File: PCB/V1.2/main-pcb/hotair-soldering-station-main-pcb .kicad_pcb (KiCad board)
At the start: 2 copper layers, 90 x 91 mm, 102 parts, among them J1 230VAC_IN, J10 T12_power (NS-25 r2,54), J11 LCD_CON2 (JST r.2.0), J12 LCD_CON1 (JST r.2.0), J13 ICP (goldpin r2,54), J14 T12_signal (NS-25 r2,54), J2 FRONT_PANEL (IDC r. 2,54), J3 EARTH_GND, J4 24V_IN (NS-25 r2,54), J5 PSUPPLY (PWZ-02S r.3,96), J6 HOTAIR_FAN (JST r,2,54), J7 HOTAIR_MEAS (JST r.2,5), J8 HOTAIR_HEATER (PWZ-02S r.3,96), J9 WEP (r.2,54), Q1 BC817, Q10 FP3055LP, Q11 BC817, Q2 BC807, Q3 BC817, Q4 Q_PMOS_GDS, Q5 BC817, Q6 BT139-600, Q7 BC817, Q8 FP3055LP, Q9 BC817, U1 MOC3041M, U2 MAX31855KASA, U3 MP1584-Step-Down, U4 AP1117-ADJ, U6 LM358, U7 MAX31855KASA, U8 STM32F103C6Tx

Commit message: Schematic and PCB update
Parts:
- removed F2: Polyfuse, Fuse:Fuse_Bourns_MF-RG500
- removed J14: T12_signal (NS-25 r2,54), Connector:Conn-01x03-N25-W4P
- removed U7: MAX31855KASA, Package_SO:SOIC-8_3.9x4.9mm_P1.27mm
- added C17: 10n, Capacitors:0805, F.Cu at (76.9, 99.7)
- added C21: 10n, Capacitors:0805, F.Cu at (84.9, 99.9)
- added C22: 100n, Capacitors:0603, F.Cu at (77.0, 94.6)
- added D1: 1N4148, Diode_SMD:D_MiniMELF, F.Cu at (161.2, 64.5)
- added D10: 1N4148, Diode_SMD:D_MiniMELF, F.Cu at (161.2, 61.3)
- added D11: 3V6, Diode_SMD:D_MiniMELF, F.Cu at (172.6, 42.0)
- added D12: SR310, Diode_SMD:D_SMA, F.Cu at (161.5, 44.7)
- added D2: 1N4148, Diode_SMD:D_MiniMELF, F.Cu at (154.8, 64.5)
- added D3: 3V6, Diode_SMD:D_MiniMELF, F.Cu at (161.1, 53.0)
- added D4: 12V, Diode_SMD:D_0805_2012Metric, F.Cu at (166.0, 51.5)
- added D6: SR310, Diode_SMD:D_SMA, F.Cu at (125.6, 42.1)
- added D8: 1N4148, Diode_SMD:D_MiniMELF, F.Cu at (154.8, 61.3)
- added D9: 12V, Diode_SMD:D_0805_2012Metric, F.Cu at (167.7, 48.4)
- added Q12: BC817, Package_TO_SOT_SMD:SOT-23, F.Cu at (161.3, 49.2)
- added Q13: BC817, Package_TO_SOT_SMD:SOT-23, F.Cu at (168.3, 38.2)
- added Q14: BC807, Package_TO_SOT_SMD:SOT-23, F.Cu at (167.9, 44.7)
- added Q15: RFP15P05, My-Footprints:TO-220-3_V_Thick_Pads, B.Cu at (112.3, 68.6)
- added R41: 1k5, Capacitors:0805, F.Cu at (64.6, 111.8)
- added R42: 430R, Capacitors:0805, F.Cu at (65.5, 106.0)
- added R43: 2k2, Capacitors:0805, F.Cu at (84.9, 97.3)
- added R44: 10k, Capacitors:0805, F.Cu at (72.7, 108.6)
- added R45: 10k, Capacitors:0805, F.Cu at (80.9, 97.3)
- added R46: 1k5, Capacitors:0805, F.Cu at (60.5, 109.1)
- added R47: 430R, Capacitors:0805, F.Cu at (85.1, 94.7)
- added R48: 1k, Capacitors:0805, F.Cu at (89.2, 94.7)
- added R49: 200k, Capacitors:0805, F.Cu at (76.9, 102.4)
- added R50: 100R, Capacitors:0805, F.Cu at (64.6, 109.1)
- added R51: 100k, Capacitors:0805, F.Cu at (73.6, 106.0)
- added R52: 10k, Capacitors:0805, F.Cu at (81.7, 105.2)
- added R53: 10k, Capacitors:0805, F.Cu at (84.9, 102.6)
- added R54: 10k, Capacitors:0805, F.Cu at (68.6, 108.6)
- added R55: 10k, Capacitors:0805, F.Cu at (76.9, 97.1)
- added R56: 47k, Capacitors:0805, F.Cu at (60.5, 111.8)
- C15: value 330u/35V -> 10n; footprint Capacitors_ThroughHole:CP_Radial_D10.0mm_P5.00mm -> Capacitors:0805; moved to F.Cu
- F1: value 3,15A -> 1,5A
- J3: footprint My-Footprints:Screw-Terminal-5.00mm-2pin -> My-Footprints:Screw-Terminal-5.00mm-3pin; moved to F.Cu
- Q10: value FP3055LP -> RFP15P05; footprint Package_TO_SOT_THT:TO-220-3_Vertical -> My-Footprints:TO-220-3_V_Thick_Pads
- Q4: value Q_PMOS_GDS -> RFP15P05
- Q8: value FP3055LP -> BC807; footprint Package_TO_SOT_THT:TO-220-3_Vertical -> Package_TO_SOT_SMD:SOT-23; moved to F.Cu
- R1: value 0R -> 47k
- R14: value xx -> 33k
- R15: value xx -> 2k2
- R16: value 0R -> 1M
- R18, R30: value 1k -> 10k
- R19: value 10k -> 1k
- R20: value 4,7k -> 2k2
- R24: value 1k -> 100k
- R27: moved to F.Cu
- R28: value 4,7k -> 200k
- R29: value 10k -> 2k2
- R32: value 100R -> 10k
- R35: value 10k -> 1M
- R36: value 1k -> 2k2
- R38: value xx -> 24k
- R40: value xx -> 2k
- moved D5 80.5 mm to (137.0, 101.6)
- moved U2 76.6 mm to (161.7, 39.2), turned to 0 degrees
- moved Q5 75.7 mm to (173.2, 38.2)
- moved R27 75.3 mm to (60.1, 106.2)
- moved J3 67.7 mm to (59.3, 94.1)
- moved LS1 64.2 mm to (62.8, 53.5), turned to -90 degrees
- moved C15 63.3 mm to (80.9, 99.9), turned to 0 degrees
- moved G*** 61.7 mm to (156.7, 81.9)
- moved R30 60.8 mm to (69.5, 106.0), turned to 0 degrees
- moved R28 60.3 mm to (68.6, 111.3), turned to 0 degrees
- moved U6 55.0 mm to (121.7, 89.9), turned to 90 degrees
- moved R32 54.3 mm to (77.6, 105.2), turned to 0 degrees
- moved C6 53.5 mm to (141.9, 92.2)
- moved C12 53.5 mm to (129.5, 99.3)
- moved C13 53.5 mm to (128.0, 99.3)
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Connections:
- C15 pad 1: +24V -> IRON_WEP_HEATER_CTRL
- C15 pad 2: GND2 -> Net-(Q7-Pad1)
- C3 pad 1: Net-(C3-Pad1) -> Net-(U6-Pad3)
- C4 pad 1: IRON_T12_THERM -> Net-(C4-Pad1)
- J10 pad 1: +24V -> Net-(J10-Pad1)
- J10 pad 2: +24V -> GND2
- J10 pad 3: IRON_T12_HEATER -> GND2
- J10 pad 4: IRON_T12_HEATER -> IRON_T12_THERM_HEATER
- J10 pad 5: IRON_T12_HEATER -> IRON_T12_THERM_HEATER
- J4 pad 3: Net-(F2-Pad2) -> +24V
- J4 pad 4: Net-(F2-Pad2) -> +24V
- J7 pad 3: HOTAIR_REED_SW -> Net-(J7-Pad3)
- J9 pad 1: +24V -> GND2
- J9 pad 2: +24V -> GND2
- J9 pad 5: IRON_WEP_THERM -> IRON_WEP_THERM+
- J9 pad 6: THERM_GND -> IRON_WEP_THERM-
- Q10 pad 1: Net-(Q10-Pad1) -> IRON_WEP_HEATER
- Q10 pad 2: IRON_T12_HEATER -> Net-(R24-Pad2)
- Q10 pad 3: GND2 -> +24V
- Q5 pad 1: Net-(Q5-Pad1) -> Net-(Q7-Pad3)
- Q5 pad 2: GND -> Net-(R25-Pad1)
- Q5 pad 3: Net-(Q5-Pad3) -> +24V
- Q7 pad 2: GND -> Net-(Q7-Pad2)
- Q8 pad 1: Net-(Q8-Pad1) -> Net-(Q7-Pad3)
- Q8 pad 2: IRON_WEP_HEATER -> Net-(R25-Pad1)
- Q8 pad 3: GND2 -> GND
- R1 pad 1: HOTAIR_THERM -> GND
- R1 pad 2: Net-(R1-Pad2) -> Net-(Q1-Pad1)
- R16 pad 1: HOTAIR_THERM -> +5V
- R16 pad 2: Net-(C3-Pad1) -> HOTAIR_THERM
- R18 pad 1: Net-(R18-Pad1) -> HOTAIR_THERM
- R18 pad 2: HOTAIR_TEMP_ADC -> Net-(U6-Pad3)
- R19 pad 1: +3V3 -> GND
- R19 pad 2: Net-(C3-Pad1) -> Net-(U6-Pad2)
- R24 pad 1: +5V -> +24V
- R24 pad 2: Net-(Q7-Pad3) -> Net-(R24-Pad2)
- R25 pad 1: Net-(Q8-Pad1) -> Net-(R25-Pad1)
- R25 pad 2: Net-(Q7-Pad3) -> Net-(R24-Pad2)
- R28 pad 1: Net-(Q5-Pad1) -> Net-(U6-Pad2)
- R28 pad 2: IRON_T12_HEATER_CTRL -> Net-(U6-Pad1)
- R29 pad 1: GND -> Net-(U6-Pad1)
- R29 pad 2: Net-(Q5-Pad1) -> HOTAIR_TEMP_ADC
- R30 pad 1: +5V -> HOTAIR_REED_SW
- R30 pad 2: Net-(Q5-Pad3) -> Net-(J7-Pad3)
- R32 pad 1: Net-(Q10-Pad1) -> Net-(J7-Pad3)
- R32 pad 2: Net-(Q5-Pad3) -> +5V
- R35 pad 1: +3V3 -> +5V
- R35 pad 2: IRON_T12_THERM -> IRON_T12_THERM_HEATER
- U2 pad 2: THERM_GND -> IRON_WEP_THERM-
- U2 pad 3: Net-(R1-Pad2) -> IRON_WEP_THERM+
- U2 pad 6: MAX31855_HOTAIR_CS -> MAX31855_IRON_CS
- U6 pad 1: Net-(R18-Pad1) -> Net-(U6-Pad1)
- U6 pad 2: Net-(R18-Pad1) -> Net-(U6-Pad2)
- U6 pad 3: Net-(C3-Pad1) -> Net-(U6-Pad3)
- U6 pad 5: IRON_T12_THERM -> Net-(C4-Pad1)
- U6 pad 6: Net-(R36-Pad1) -> Net-(U6-Pad6)
- U8 pad 14: MAX31855_HOTAIR_CS -> unconnected-(U8-Pad14)
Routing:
- net +3V3: track 187.0 -> 0.00 mm, vias 9 -> 0
- net +5V: track 183.2 -> 0.00 mm, vias 2 -> 0
- net HOTAIR_FAN_ADC: track 120.1 -> 0.00 mm, vias 4 -> 0
- net AC_230(N): track 110.7 -> 0.00 mm
- net HOTAIR_REED_SW: track 93.2 -> 0.00 mm, vias 3 -> 0
- net +24V: track 85.2 -> 0.00 mm
- net THERM_GND: track 84.7 -> 0.00 mm, vias 5 -> 0
- net GND2: track 84.0 -> 0.00 mm, vias 1 -> 0
- net SWDIO: track 79.1 -> 0.00 mm, vias 3 -> 0
- net SWCLK: track 77.4 -> 0.00 mm, vias 2 -> 0
- net HOTAIR_THERM: track 75.0 -> 0.00 mm, vias 2 -> 0
- net IRON_WEP_HEATER_CTRL: track 68.4 -> 0.00 mm, vias 6 -> 0
- net HOTAIR_HEATER_CTRL: track 59.7 -> 0.00 mm
- net HOTAIR_FAN_PWM: track 59.1 -> 0.00 mm, vias 2 -> 0
- net HOTAIR_UP_SW: track 55.1 -> 0.00 mm, vias 2 -> 0
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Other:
- board size 90 x 91 mm -> 120.3 x 65.7 mm

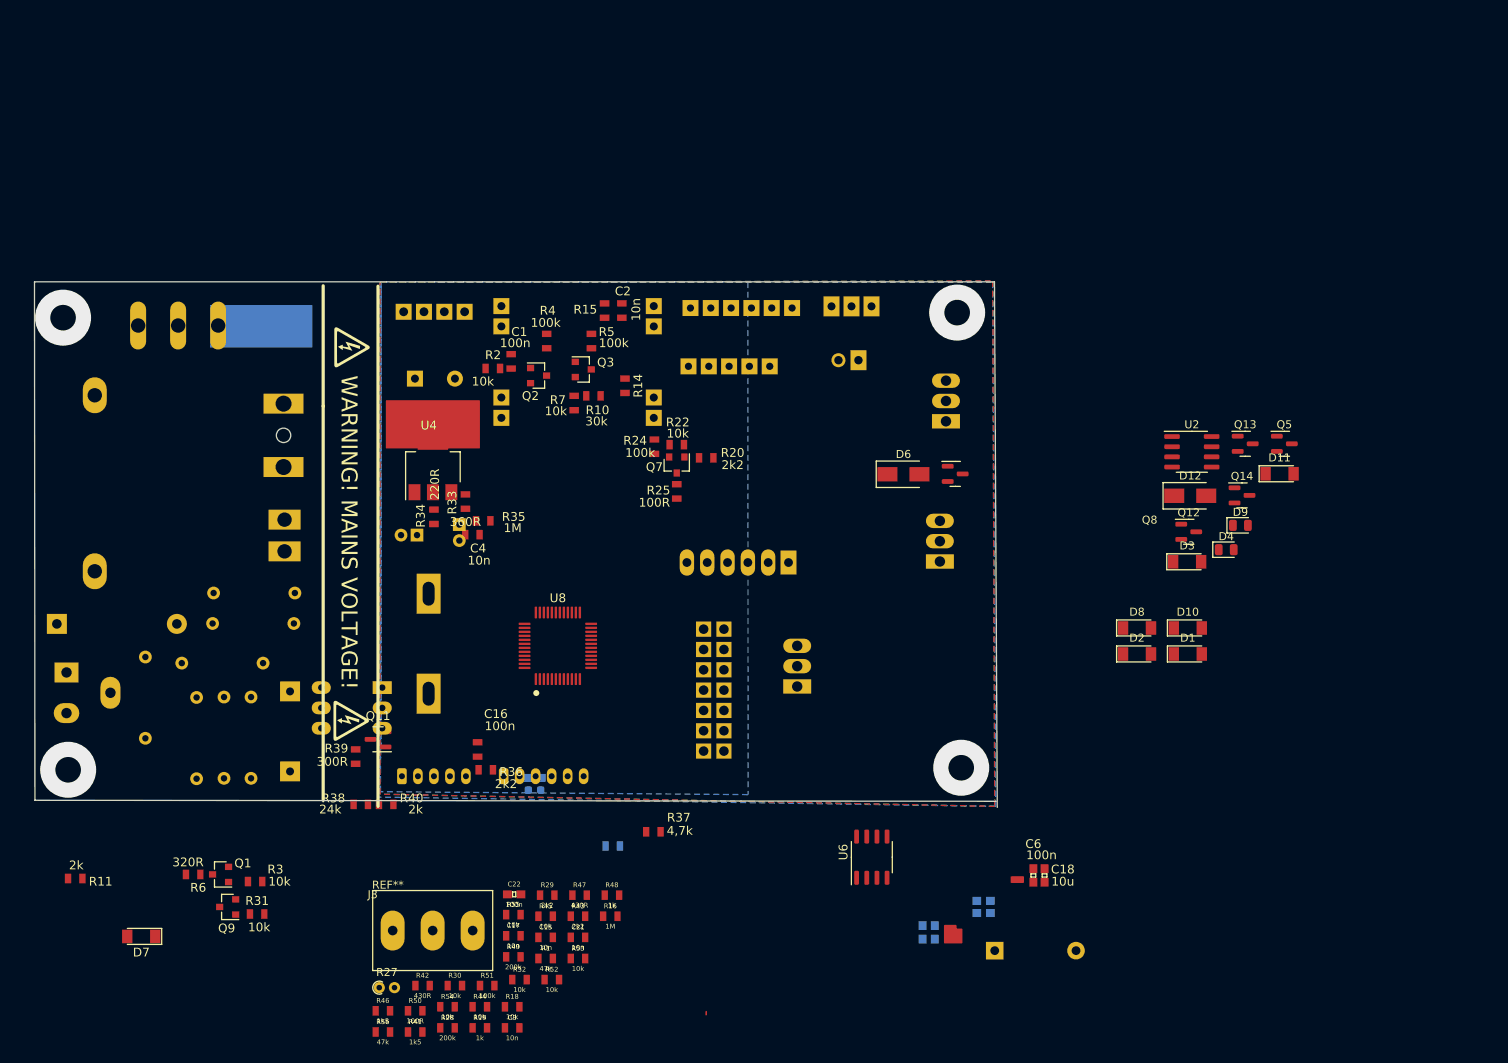
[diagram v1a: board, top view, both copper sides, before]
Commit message: All knowned problems fixed on schematic, routing mains voltage section
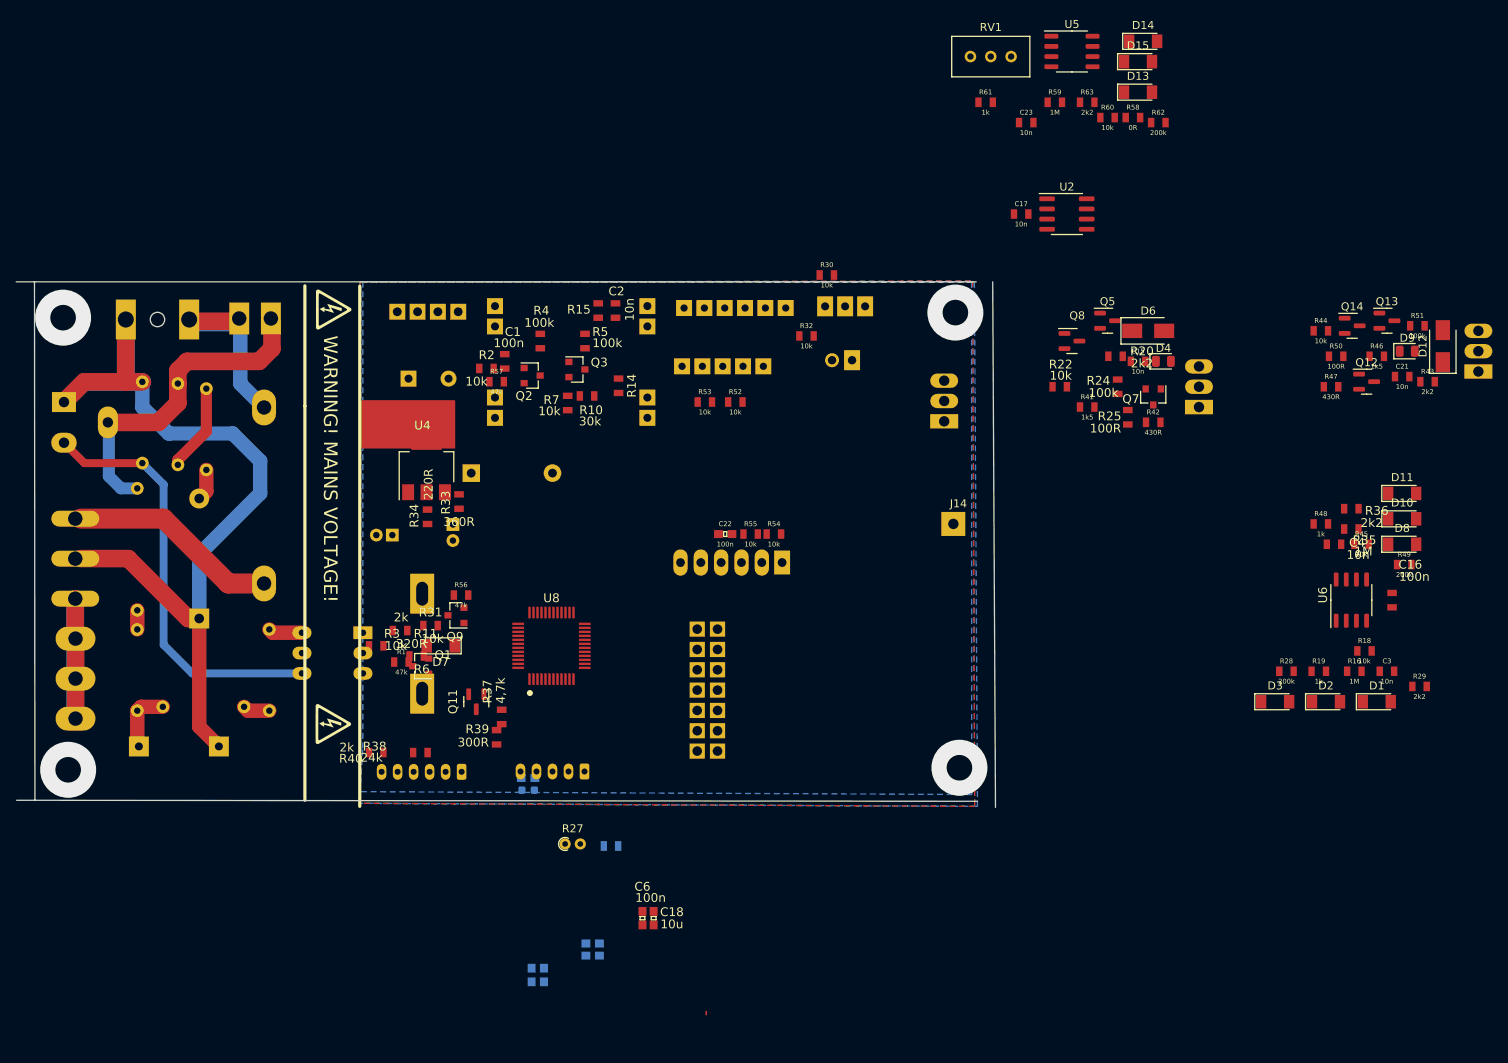
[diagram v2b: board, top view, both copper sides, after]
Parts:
- added C23: 10n, Capacitors:0805, F.Cu at (141.0, -1.91)
- added D13: 1N4148, Diode_SMD:D_MiniMELF, F.Cu at (154.9, -5.71)
- added D14: 1N4148, Diode_SMD:D_MiniMELF, F.Cu at (155.6, -12.1)
- added D15: 3V6, Diode_SMD:D_MiniMELF, F.Cu at (154.9, -9.53)
- added J14: Unused_GPIO, My-Footprints:WIRE_PAD_1,3mm, F.Cu at (131.9, 48.3)
- added R57: 47k, Capacitors:0805, F.Cu at (74.8, 30.5)
- added R58: 0R, Resistors:0805, F.Cu at (154.3, -2.54)
- added R59: 1M, Capacitors:0805, F.Cu at (144.6, -4.45)
- added R60: 10k, Capacitors:0805, F.Cu at (151.1, -2.54)
- added R61: 1k, Capacitors:0805, F.Cu at (135.9, -4.45)
- added R62: 200k, Capacitors:0805, F.Cu at (157.5, -1.91)
- added R63: 2k2, Capacitors:0805, F.Cu at (148.6, -4.45)
- added RV1: 10k, Potentiometer_THT:Potentiometer_Bourns_3296W_Vertical, F.Cu at (139.1, -10.2)
- added U5: LM741, Package_SO:SO-8_3.9x4.9mm_P1.27mm, F.Cu at (146.7, -10.8)
- J3: moved to B.Cu
- R21: footprint Resistors_ThroughHole:R_Axial_DIN0207_L6.3mm_D2.5mm_P10.16mm_Horizontal -> Resistor_THT:R_Axial_DIN0207_L6.3mm_D2.5mm_P15.24mm_Horizontal
- U6: value LM358 -> AD8606
- moved G*** 158.4 mm to (0.38, 107.2)
- moved R46 148.8 mm to (184.8, 27.3)
- moved R51 142.6 mm to (189.9, 23.5)
- moved R50 141.2 mm to (179.7, 27.3)
- moved R44 134.9 mm to (177.8, 24.1)
- moved R43 125.5 mm to (191.1, 30.5)
- moved C21 124.6 mm to (188.0, 29.8)
- moved R49 121.7 mm to (188.2, 53.3)
- moved C3 118.1 mm to (186.1, 66.7)
- moved C16 115.8 mm to (186.7, 57.8)
- moved R18 115.5 mm to (183.3, 64.1)
- moved R42 115.3 mm to (156.8, 35.6)
- moved R41 114.7 mm to (148.6, 33.7)
- moved R19 113.9 mm to (177.5, 66.7)
- moved R28 113.9 mm to (173.5, 66.7)
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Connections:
- J11 pad 1: +5V -> GND
- J11 pad 2: GND -> +5V
- J11 pad 4: Net-(J11-Pad4) -> LCD_RS
- J11 pad 5: LCD_D7 -> LCD_RW
- J12 pad 1: LCD_D6 -> LCD_EN
- J12 pad 2: LCD_D5 -> LCD_D4
- J12 pad 3: LCD_D4 -> LCD_D5
- J12 pad 4: LCD_EN -> LCD_D6
- J12 pad 5: LCD_RW -> LCD_D7
- J12 pad 6: LCD_RS -> Net-(J12-Pad6)
- R38 pad 2: Net-(J11-Pad4) -> Net-(J11-Pad3)
- R39 pad 1: Net-(J11-Pad3) -> Net-(J12-Pad6)
- R40 pad 1: Net-(J11-Pad4) -> Net-(J11-Pad3)
- U3 pad 3: GND -> +5V
- U3 pad 4: +5V -> GND
- U8 pad 14: unconnected-(U8-Pad14) -> UNUSED_GPIO
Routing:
- net AC_230(N): track 0.00 -> 115.6 mm
- net Net-(Q6-Pad3): track 0.00 -> 53.4 mm
- net Net-(J8-Pad1): track 0.00 -> 40.9 mm
- net Net-(J1-Pad1): track 0.00 -> 30.0 mm
- net Net-(F1-Pad2): track 0.00 -> 26.3 mm
- net AC_230(L): track 0.00 -> 24.9 mm
- net Net-(R23-Pad2): track 0.00 -> 11.0 mm
- net Net-(C5-Pad1): track 0.00 -> 7.95 mm
- net Net-(R8-Pad1): track 0.00 -> 4.25 mm
- net Net-(C7-Pad1): track 0.00 -> 3.94 mm
- net Net-(R13-Pad1): track 0.00 -> 3.36 mm
- net Net-(R17-Pad1): track 0.00 -> 2.39 mm
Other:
- board size 120.3 x 65.7 mm -> 122.4 x 65.7 mm
- board text added: "LED BCL"
- board text removed: "230V INPUT"
- board text removed: "EARTH"
- board text removed: "HOTAIR HEATER"
- board text removed: "POWER SUPPLY 230v MAINS"

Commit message: Routing PCB
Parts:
- C18, C6, R33, R34, U4: moved to B.Cu
- C19, C9: moved to F.Cu
- moved R9 97.1 mm to (63.4, -5.08)
- moved Q15 72.8 mm to (127.5, 49.3)
- moved R50 72.8 mm to (109.7, 47.4)
- moved C21 72.8 mm to (118.0, 49.9)
- moved Q13 72.8 mm to (116.1, 42.9)
- moved Q14 72.8 mm to (111.7, 43.6)
- moved R44 72.8 mm to (107.8, 44.2)
- moved R46 72.8 mm to (114.8, 47.4)
- moved R51 72.8 mm to (119.9, 43.6)
- moved D12 72.8 mm to (123.1, 46.1)
- moved D9 72.8 mm to (118.6, 46.7)
- moved Q12 72.8 mm to (113.5, 50.5)
- moved R43 72.8 mm to (121.2, 50.5)
- moved R47 72.8 mm to (109.1, 51.2)
- moved C2 62.2 mm to (119.1, 76.3), turned to 0 degrees
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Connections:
- J4 pad 1: GND -> GND2
- J4 pad 2: GND -> GND2
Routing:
- net +3V3: track 0.00 -> 102.0 mm, vias 0 -> 2
- net +5V: track 0.00 -> 101.4 mm, vias 0 -> 2
- net SWDIO: track 0.00 -> 60.6 mm, vias 0 -> 1
- net SWCLK: track 0.00 -> 47.8 mm, vias 0 -> 1
- net HOTAIR_FAN_DOWN_SW: track 0.00 -> 41.3 mm
- net HOTAIR_UP_SW: track 0.00 -> 37.7 mm
- net HOTAIR_ON_SW: track 0.00 -> 36.5 mm
- net RST: track 0.00 -> 33.9 mm, vias 0 -> 1
- net SOLDER_ON_SW: track 0.00 -> 32.2 mm
- net HOTAIR_FAN_UP_SW: track 0.00 -> 31.3 mm
- net HOTAIR_FAN_ADC: track 0.00 -> 30.7 mm, vias 0 -> 1
- net LCD_D7: track 0.00 -> 30.3 mm
- net HOTAIR_HEATER_CTRL: track 0.00 -> 28.4 mm
- net LCD_D6: track 0.00 -> 27.7 mm
- net UART_DBG_TX: track 0.00 -> 26.4 mm, vias 0 -> 2
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- added copper zone on B.Cu, net GND2
- added copper zone on F.Cu, net GND2
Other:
- board size 122.4 x 65.7 mm -> 120.1 x 65.7 mm
- board text added: "HOTAIR"
- board text added: "POWER SUPPLY"

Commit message: Routing PCB
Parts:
- D12, D6: moved to B.Cu
- RV1: footprint Potentiometer_THT:Potentiometer_Bourns_3296W_Vertical -> Potentiometer_SMD:Potentiometer_Bourns_3224W_Vertical
- moved D10 128.6 mm to (59.7, 37.5), turned to 90 degrees
- moved D11 127.2 mm to (60.8, 45.5)
- moved D8 126.3 mm to (62.3, 37.6), turned to -90 degrees
- moved R49 126.1 mm to (62.6, 42.3), turned to -90 degrees
- moved R29 122.9 mm to (69.1, 46.8)
- moved C16 122.3 mm to (64.9, 46.0), turned to -90 degrees
- moved R36 121.6 mm to (60.0, 43.3), turned to 180 degrees
- moved R45 118.4 mm to (65.1, 39.0), turned to 180 degrees
- moved R48 118.0 mm to (60.0, 41.6)
- moved C4 117.8 mm to (64.5, 36.6), turned to 90 degrees
- moved C3 116.9 mm to (72.5, 39.0), turned to 90 degrees
- moved U6 115.1 mm to (67.5, 42.6), turned to 180 degrees
- moved D1 115.1 mm to (74.4, 37.8), turned to -90 degrees
- moved R18 112.4 mm to (73.1, 41.6), turned to 180 degrees
- moved R35 112.4 mm to (67.7, 38.2), turned to 90 degrees
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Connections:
- R32 pad 2: +5V -> +3V3
- R53 pad 2: +5V -> unconnected-(R53-Pad2)
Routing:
- net +24V: track 8.04 -> 73.7 mm
- net +3V3: track 102.0 -> 125.8 mm, vias 2 -> 4
- net HOTAIR_HEATER_CTRL: track 28.4 -> 45.5 mm, vias 0 -> 2
- net Net-(C3-Pad1): track 0.00 -> 8.59 mm
- net Net-(C4-Pad1): track 0.00 -> 8.49 mm
- net GND: track 7.12 -> 14.1 mm, vias 8 -> 16
- net +5V: track 101.4 -> 96.2 mm
- net Net-(Q15-Pad2): track 0.00 -> 4.75 mm
- net Net-(R48-Pad2): track 0.00 -> 4.32 mm
- net Net-(R36-Pad1): track 0.00 -> 4.07 mm
- net IRON_T12_THERM_HEATER: track 0.00 -> 3.23 mm
- net IRON_WEP_HEATER: track 0.00 -> 2.54 mm
- net HOTAIR_THERM: track 0.00 -> 2.26 mm
- net IRON_T12_TEMP_ADC: track 0.00 -> 2.20 mm
- net MENU_DOWN_SW: track 14.8 -> 16.6 mm
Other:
- board size 120.1 x 65.7 mm -> 100 x 65 mm

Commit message: Routing PCB
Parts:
- D6: moved to F.Cu
- RV1: footprint Potentiometer_SMD:Potentiometer_Bourns_3224W_Vertical -> Potentiometer_SMD:Potentiometer_Bourns_3314G_Vertical
- moved R32 64.7 mm to (160.1, 18.0)
- moved R30 64.7 mm to (157.0, 18.0)
- moved D14 42.8 mm to (140.3, 24.4)
- moved R58 42.8 mm to (139.4, 29.7)
- moved D13 42.8 mm to (142.7, 24.4)
- moved RV1 42.8 mm to (135.5, 27.6)
- moved R59 42.6 mm to (136.9, 39.6)
- moved R61 42.6 mm to (133.1, 40.5)
- moved R63 42.6 mm to (136.9, 41.5)
- moved U5 42.6 mm to (136.8, 35.6)
- moved C23 42.6 mm to (141.6, 33.5)
- moved D15 42.6 mm to (142.7, 41.1)
- moved R60 42.6 mm to (141.6, 36.7)
- moved R62 42.6 mm to (131.8, 36.2)
- moved U3 34.8 mm to (57.1, 38.7), turned to 0 degrees
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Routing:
- net IRON_T12_THERM_HEATER: track 3.23 -> 47.5 mm
- net IRON_WEP_HEATER: track 2.54 -> 16.4 mm
- net Net-(Q10-Pad2): track 0.00 -> 8.80 mm
- net Net-(D4-Pad1): track 0.00 -> 6.08 mm
- net Net-(C15-Pad2): track 0.00 -> 5.17 mm
- net Net-(C4-Pad1): track 8.49 -> 5.88 mm
- net Net-(Q7-Pad2): track 0.00 -> 2.40 mm
- net IRON_WEP_HEATER_CTRL: track 0.00 -> 1.78 mm
- net MENU_UP_SW: track 24.7 -> 23.2 mm
- net Net-(Q5-Pad2): track 0.37 -> 1.87 mm
- net HOTAIR_UP_SW: track 37.4 -> 36.5 mm
- net SOLDER_DOWN_SW: track 17.2 -> 16.5 mm
- net SOLDER_ON_SW: track 31.9 -> 31.2 mm
- net MENU_DOWN_SW: track 16.6 -> 15.9 mm
- net GND: vias 16 -> 13
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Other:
- board size 100 x 65 mm -> 100 x 70 mm

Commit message: Routing PCB
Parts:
- moved R32 99.6 mm to (60.6, 19.5), turned to -90 degrees
- moved R30 94.4 mm to (62.5, 19.5), turned to 90 degrees
- moved D13 82.8 mm to (60.1, 29.5), turned to 90 degrees
- moved D14 78.3 mm to (62.2, 29.5), turned to -90 degrees
- moved R58 73.5 mm to (65.9, 30.0), turned to 90 degrees
- moved D15 72.0 mm to (73.4, 21.8), turned to 180 degrees
- moved R63 70.1 mm to (70.4, 19.4)
- moved R61 70.1 mm to (65.8, 21.0), turned to -90 degrees
- moved U5 69.1 mm to (68.3, 25.9), turned to 0 degrees
- moved R60 66.9 mm to (75.2, 28.7), turned to -90 degrees
- moved C23 66.4 mm to (75.2, 32.1), turned to -90 degrees
- moved RV1 65.8 mm to (70.0, 33.2), turned to 0 degrees
- moved R62 64.9 mm to (68.6, 21.8), turned to 0 degrees
- moved R59 64.3 mm to (74.3, 25.1), turned to -90 degrees
- moved U3 28.9 mm to (80.0, 21.0), turned to 180 degrees
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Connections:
- R53 pad 2: unconnected-(R53-Pad2) -> +3V3
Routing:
- net FAN_SUPPLY: track 0.00 -> 76.3 mm, vias 0 -> 2
- net HOTAIR_REED_SW: track 0.00 -> 71.9 mm, vias 0 -> 2
- net IRON_WEP_THERM-: track 0.00 -> 57.3 mm, vias 0 -> 2
- net IRON_T12_TEMP_ADC: track 2.20 -> 58.1 mm, vias 0 -> 2
- net IRON_WEP_THERM+: track 0.00 -> 53.0 mm, vias 0 -> 2
- net +5V: track 96.2 -> 147.5 mm
- net MAX31855_IRON_CS: track 0.00 -> 45.0 mm, vias 0 -> 3
- net IRON_WEP_HEATER_CTRL: track 1.78 -> 41.4 mm, vias 0 -> 2
- net HOTAIR_THERM: track 2.26 -> 36.7 mm, vias 0 -> 1
- net IRON_T12_THERM_HEATER: track 47.5 -> 81.6 mm
- net THERM_GND: track 0.00 -> 31.0 mm
- net +24V: track 73.4 -> 98.6 mm
- net SPI1_MISO: track 0.00 -> 22.4 mm, vias 0 -> 1
- net +3V3: track 125.8 -> 146.4 mm, vias 4 -> 5
- net Net-(C23-Pad1): track 0.00 -> 19.4 mm, vias 0 -> 2
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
